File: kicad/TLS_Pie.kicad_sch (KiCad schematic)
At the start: 21 parts, among them M1 stepper + 50:1, U1 DS3231 breakout, U10 fan 5 V, U11 INA226 -- NOT FITTED, U12 BCD5A -> 16.8 V / 1.5 A, U3 LM2596S-ADJ -> 5.1 V, U4 Big Easy Driver, U7 VLP-16 interface box, U8 Velodyne VLP-16

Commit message: Add D1: the charge chain was draining the pack backwards through its own LED
Caught live rather than reasoned about.  With the USB unplugged but the buck
still wired to the BMS, the pack fed BACKWARDS through the buck -- out of the
pack, through the inductor, through the switch's body diode to the input --
and lit the buck's own indicator LED.  The pack was going down while
everything looked idle.

A few mA is ~1.7 Ah a week on a ~9 Ah pack, and this pack has already been
flattened once by exactly this class of fault, so this is not a rounding
error.  It is the same failure wearing a different component.

Fix is an SS54 Schottky in the charge lead.  A connector there would also work
and costs no volts, but it can be forgotten and a diode cannot.

Consequence, and it matters: the buck now wants 17.0 V open-circuit, not 16.8.
At taper current the Schottky drops ~0.2 V so the PACK lands at ~16.8 V, which
is what the balancer needs -- it only bleeds near 4.2 V/cell, so an
undercharged pack never balances and the weak group never gets found.  If D1 is
ever bypassed, 17.0 V is 4.25 V/cell and the BMS's 4.2 V/cell over-voltage
cutoff is the backstop.  That is what it is for.

Verified: 2139 validator checks 0 failed; KiCad ERC 0 violations.

Co-Authored-By: Claude Opus 5 <noreply@anthropic.com>
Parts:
- added D1: SS54 -- blocks back-feed, symbol TLS_Pie:Diode
- U12: value BCD5A -> 16.8 V / 1.5 A -> BCD5A -> 17.0 V / 1.5 A
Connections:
- net +VBATT: now also D1.2 (K); no longer U12.1 (OUT+)
- new net: D1.1 (A), U12.1 (OUT+)

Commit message: D1 is 1N5822, not SS54 -- I specified a surface-mount part for a hand-wired job
Any Schottky of >=3 A and >=30 V does the job: 1N5822, SB540, SR360, MBR340.
SS54 is DO-214AB, which is the wrong shape for this build entirely.  Not a
1N400x either -- silicon drops ~1 V instead of ~0.2 and the 17.0 V sum stops
working.

Also recorded: the free alternative is a connector or switch in the same lead,
BETWEEN the buck and the pack.  Unplugging the USB is what causes the
back-feed, so the break has to be on the pack side.  It costs no volts and can
be forgotten, which is the whole argument for the diode.

And this does not block tonight: the pack can be charged now by physically
disconnecting the buck from the BMS when it finishes.  The drain only happens
when the buck is left on the pack with no USB power.

Co-Authored-By: Claude Opus 5 <noreply@anthropic.com>
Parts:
- D1: value SS54 -- blocks back-feed -> 1N5822 -- BANDED END TO THE PACK

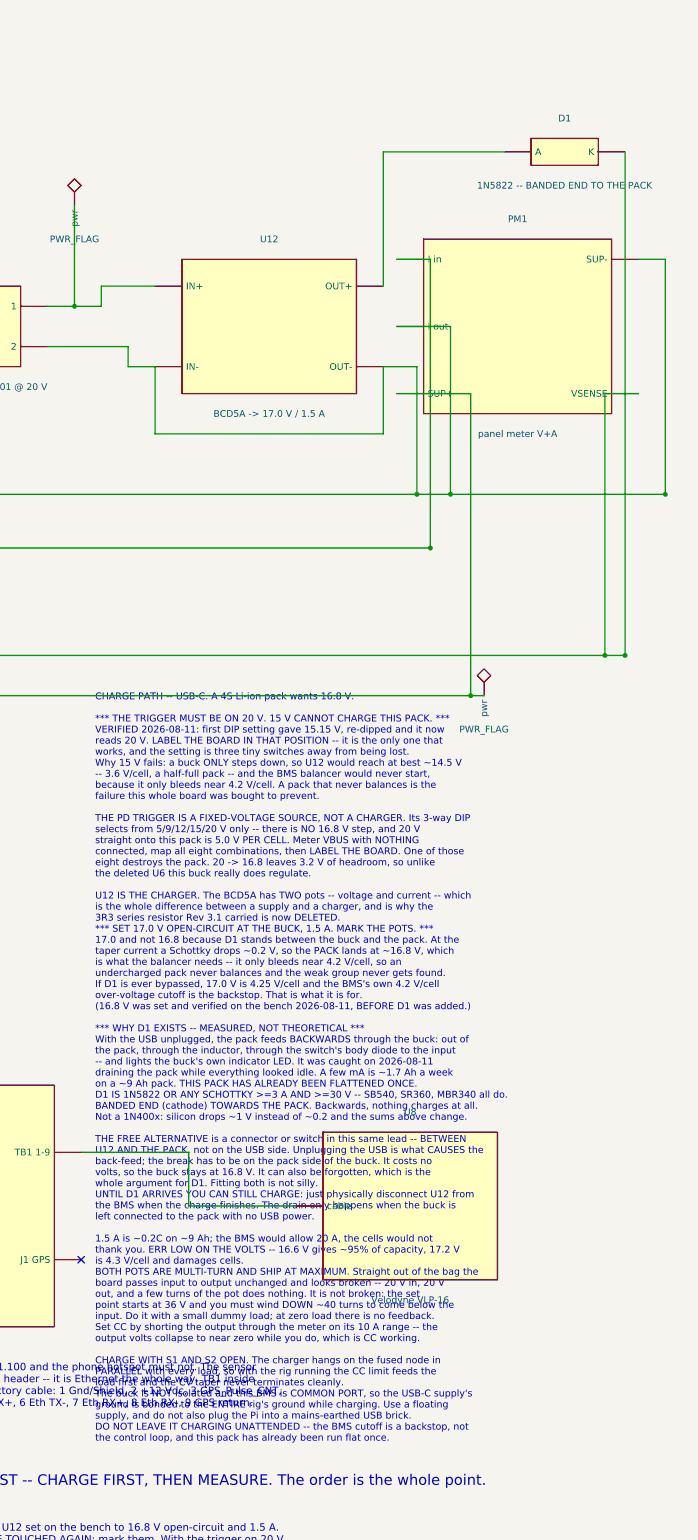
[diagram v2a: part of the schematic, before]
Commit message: S3 charge-isolate switch fitted; D1 drawn DNP until it arrives
The switch solves the back-feed today and costs no volts, so the buck stays at
the 16.8 V already set and verified.  D1 stays on the sheet as not-fitted
rather than being dropped, because the two are not interchangeable: a switch
can be forgotten and a diode cannot.  Keep both.

The placement rule is the part worth not losing.  S3 has to sit between the
buck and the pack, never on the USB side -- unplugging the USB is what CAUSES
the back-feed, so the break must be on the pack side of the buck.

New assertion: S3 must actually BREAK the charge path.  If its two sides ever
end up one node it isolates nothing and the drain that flattened this pack
walks straight through it, silently, exactly as before.

Buck voltage now has a condition attached: 16.8 V while S3 is the only
isolation, 17.0 V once D1 is in.  Written on the sheet next to both.

Verified: 2186 validator checks 0 failed; KiCad ERC 0 violations.

Co-Authored-By: Claude Opus 5 <noreply@anthropic.com>
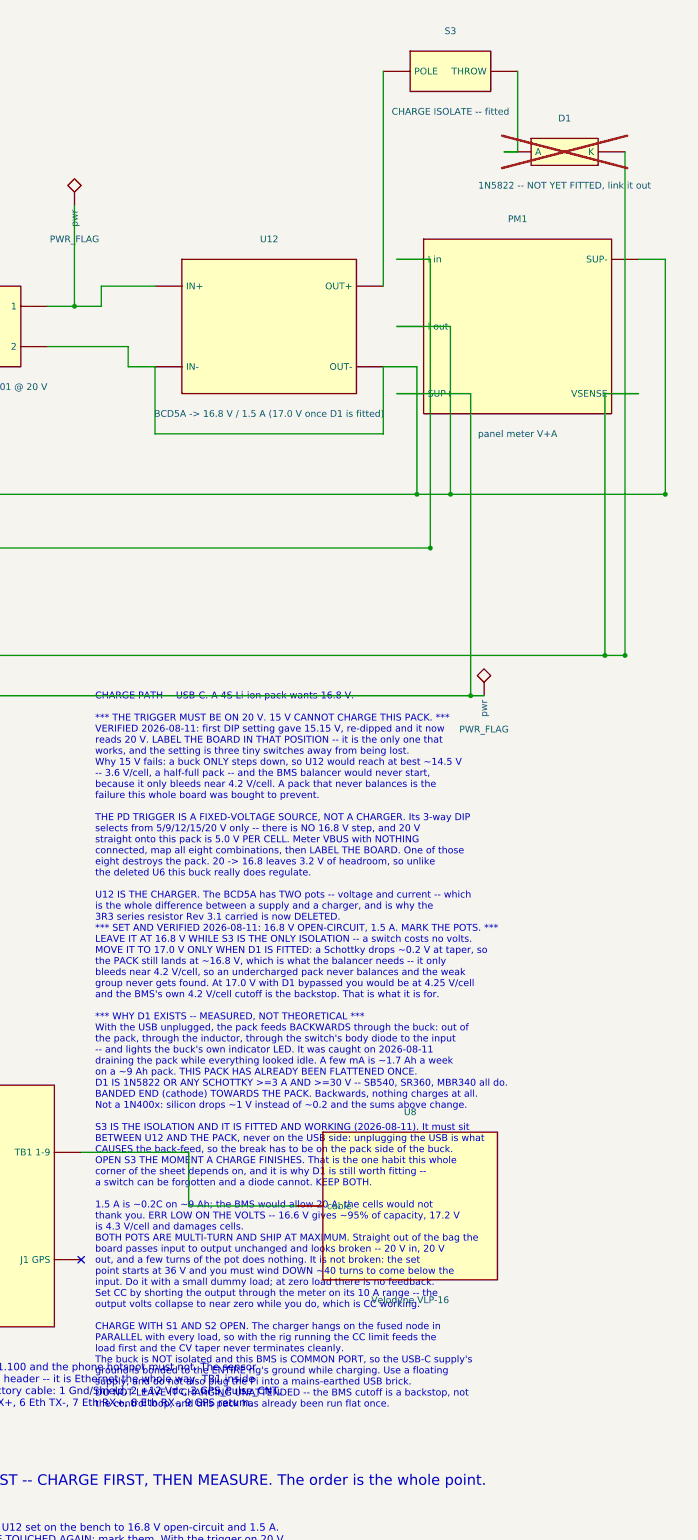
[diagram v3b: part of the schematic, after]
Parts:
- added S3: CHARGE ISOLATE -- fitted, symbol TLS_Pie:SW_SPST
- D1: value 1N5822 -- BANDED END TO THE PACK -> 1N5822 -- NOT YET FITTED, link it out; now not fitted
- U12: value BCD5A -> 17.0 V / 1.5 A -> BCD5A -> 16.8 V / 1.5 A (17.0 V once D1 is fitted)
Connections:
- net at U12.1 (OUT+): now also S3.1 (POLE); no longer D1.1 (A)
- new net: D1.1 (A), S3.2 (THROW)
